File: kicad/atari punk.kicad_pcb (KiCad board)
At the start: 2 copper layers, 66 x 33 mm, 20 parts, among them J1 JACK_2P, J2 JACK_2P, J3 JACK_2P, P9v1 CONN_2, SW1 DUAL_SWITCH_INV, U1 LM555N, U2 LM555N

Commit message: Added missing tracks, made GND and Vin tracks 0.6mm.
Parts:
- moved R2 2.54 mm to (123.2, 101.6), turned to 270 degrees
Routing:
- net N-000001: track 6.66 -> 25.1 mm
- net GND: track 98.1 -> 108.6 mm
- net N-0000015: track 5.24 -> 7.40 mm
- net N-000004: track 10.4 -> 8.89 mm
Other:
- net class Vin added: clearance 0.254, trace_width 0.6, via_dia 0.889, via_drill 0.635
- net class gnd added: clearance 0.254, trace_width 0.6, via_dia 0.889, via_drill 0.635
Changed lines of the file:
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@@
   (general
     (links 32)
-    (no_connects 4)
-    (area 0 0 0 0)
+    (no_connects 0)
+    (area 113.674286 84.459334 181.20381 119.430001)
     (thickness 1.6)
     (drawings 6)
-    (tracks 50)
+    (tracks 55)
     (zones 0)
     (modules 20)
@@
       (outputformat 1)
       (mirror false)
-      (drillshape 1)
+      (drillshape 0)
       (scaleselection 1)
       (outputdirectory ""))
@@
     (add_net /OUTPUT_A)
     (add_net /OUTPUT_B)
-    (add_net /Vin)
-    (add_net GND)
     (add_net N-000001)
     (add_net N-0000012)
@@
     (add_net VCC)
   )
+  (net_class Vin ""
+    (clearance 0.254)
+    (trace_width 0.6)
+    (via_dia 0.889)
+    (via_drill 0.635)
+    (uvia_dia 0.508)
+    (uvia_drill 0.127)
+    (add_net /Vin)
+  )
+  (net_class gnd ""
+    (clearance 0.254)
+    (trace_width 0.6)
+    (via_dia 0.889)
+    (via_drill 0.635)
+    (uvia_dia 0.508)
+    (uvia_drill 0.127)
+    (add_net GND)
+  )
   (module R1 (layer F.Cu)
-    (at 123.19 99.06 90)
+    (at 123.19 101.6 270)
     (descr "Resistance verticale")
     (tags R)
     (autoplace_cost90 10)
     (autoplace_cost180 10)
-    (fp_text reference R2 (at -1.016 2.54 90) (layer F.SilkS)
+    (fp_text reference R2 (at -1.016 2.54 270) (layer F.SilkS)
       (effects (font (size 1.397 1.27) (thickness 0.2032)))
     )
-    (fp_text value 1k (at -1.143 2.54 90) (layer F.SilkS) hide
+    (fp_text value 1k (at -1.143 2.54 270) (layer F.SilkS) hide
       (effects (font (size 1.397 1.27) (thickness 0.2032)))
     )
     (fp_line (start -1.27 0) (end 1.27 0) (layer F.SilkS) (width 0.381))
     (fp_circle (center -1.27 0) (end -0.635 1.27) (layer F.SilkS) (width 0.381))
-    (pad 1 thru_hole circle (at -1.27 0 90) (size 1.397 1.397) (drill 0.8128)
+    (pad 1 thru_hole circle (at -1.27 0 270) (size 1.397 1.397) (drill 0.8128)
       (layers *.Cu *.Mask F.SilkS)
       (net 10 N-000002)
     )
-    (pad 2 thru_hole circle (at 1.27 0 90) (size 1.397 1.397) (drill 0.8128)
+    (pad 2 thru_hole circle (at 1.27 0 270) (size 1.397 1.397) (drill 0.8128)
       (layers *.Cu *.Mask F.SilkS)
       (net 5 N-000001)
@@
   (segment (start 138.43 100.33) (end 134.62 100.33) (width 0.254) (layer B.Cu) (net 1))
   (segment (start 157.48 101.6) (end 162.56 99.06) (width 0.254) (layer B.Cu) (net 2) (status 20))
-  (segment (start 168.91 90.17) (end 143.51 90.17) (width 0.254) (layer B.Cu) (net 3) (status 10))
-  (segment (start 162.56 114.3) (end 162.56 116.84) (width 0.254) (layer B.Cu) (net 4))
-  (segment (start 154.94 114.3) (end 154.94 116.84) (width 0.254) (layer B.Cu) (net 4))
-  (segment (start 163.83 116.84) (end 162.56 116.84) (width 0.254) (layer B.Cu) (net 4))
-  (segment (start 171.45 92.71) (end 171.45 109.22) (width 0.254) (layer B.Cu) (net 4))
-  (segment (start 171.45 109.22) (end 171.45 116.84) (width 0.254) (layer B.Cu) (net 4))
-  (segment (start 171.45 116.84) (end 163.83 116.84) (width 0.254) (layer B.Cu) (net 4))
-  (segment (start 162.56 116.84) (end 154.94 116.84) (width 0.254) (layer B.Cu) (net 4))
-  (segment (start 154.94 116.84) (end 134.62 116.84) (width 0.254) (layer B.Cu) (net 4))
-  (segment (start 134.62 116.84) (end 134.62 114.3) (width 0.254) (layer B.Cu) (net 4) (status 20))
-  (segment (start 171.45 92.71) (end 171.45 90.17) (width 0.254) (layer B.Cu) (net 4))
-  (segment (start 162.56 92.71) (end 171.45 92.71) (width 0.254) (layer B.Cu) (net 4))
-  (segment (start 162.56 114.3) (end 157.48 106.68) (width 0.254) (layer B.Cu) (net 4) (status 10))
+  (segment (start 143.51 90.17) (end 168.91 90.17) (width 0.6) (layer B.Cu) (net 3) (status C00000))
+  (segment (start 162.56 107.95) (end 158.75 107.95) (width 0.6) (layer B.Cu) (net 4) (status 400000))
+  (segment (start 158.75 107.95) (end 157.48 106.68) (width 0.6) (layer B.Cu) (net 4) (status 800000))
+  (segment (start 154.94 114.3) (end 154.94 116.84) (width 0.6) (layer B.Cu) (net 4) (status 400000))
+  (segment (start 162.56 116.84) (end 162.56 114.3) (width 0.6) (layer B.Cu) (net 4) (status 800000))
+  (segment (start 134.62 114.3) (end 134.62 105.41) (width 0.6) (layer B.Cu) (net 4) (status C00000))
+  (segment (start 171.45 90.17) (end 171.45 116.84) (width 0.6) (layer B.Cu) (net 4) (status 400000))
+  (segment (start 134.62 116.84) (end 134.62 114.3) (width 0.6) (layer B.Cu) (net 4) (status 800000))
+  (segment (start 171.45 116.84) (end 162.56 116.84) (width 0.6) (layer B.Cu) (net 4))
+  (segment (start 162.56 116.84) (end 154.94 116.84) (width 0.6) (layer B.Cu) (net 4))
+  (segment (start 154.94 116.84) (end 134.62 116.84) (width 0.6) (layer B.Cu) (net 4))
+  (segment (start 171.45 90.17) (end 171.45 92.71) (width 0.6) (layer B.Cu) (net 4) (status 400000))
+  (segment (start 171.45 92.71) (end 162.56 92.71) (width 0.6) (layer B.Cu) (net 4) (status 800000))
+  (segment (start 162.56 114.3) (end 162.56 111.76) (width 0.6) (layer B.Cu) (net 4) (status 400000))
+  (segment (start 162.56 111.76) (end 157.48 106.68) (width 0.6) (layer B.Cu) (net 4) (status 800000))
+  (segment (start 158.75 107.95) (end 157.48 106.68) (width 0.254) (layer B.Cu) (net 4))
   (segment (start 134.62 114.3) (end 134.62 114.3) (width 0.254) (layer B.Cu) (net 4) (status 30))
-  (segment (start 134.62 105.41) (end 134.62 114.3) (width 0.254) (layer B.Cu) (net 4) (status 20))
-  (segment (start 123.19 97.79) (end 123.19 96.52) (width 0.254) (layer B.Cu) (net 5))
+  (segment (start 127 102.87) (end 130.81 99.06) (width 0.254) (layer B.Cu) (net 5))
+  (segment (start 130.81 96.52) (end 127 92.71) (width 0.254) (layer B.Cu) (net 5))
+  (segment (start 130.81 99.06) (end 130.81 96.52) (width 0.254) (layer B.Cu) (net 5))
   (segment (start 123.19 96.52) (end 127 92.71) (width 0.254) (layer B.Cu) (net 5))
+  (segment (start 123.19 102.87) (end 123.19 96.52) (width 0.254) (layer B.Cu) (net 5) (status 10))
   (segment (start 143.51 104.14) (end 149.86 104.14) (width 0.254) (layer B.Cu) (net 6))
   (segment (start 143.51 109.22) (end 143.51 104.14) (width 0.254) (layer B.Cu) (net 6) (status 10))
@@
   (segment (start 143.51 114.3) (end 149.86 114.3) (width 0.254) (layer B.Cu) (net 7) (status 20))
   (segment (start 123.19 113.03) (end 129.54 114.3) (width 0.254) (layer B.Cu) (net 8) (status 20))
+  (segment (start 167.64 114.3) (end 167.64 110.49) (width 0.254) (layer B.Cu) (net 9))
+  (segment (start 167.64 110.49) (end 165.1 107.95) (width 0.254) (layer B.Cu) (net 9))
   (segment (start 167.64 114.3) (end 167.64 114.3) (width 0.254) (layer B.Cu) (net 9) (status 30))
-  (segment (start 165.1 107.95) (end 166.37 102.87) (width 0.254) (layer B.Cu) (net 9) (status 10))
-  (segment (start 127 100.33) (end 123.19 100.33) (width 0.254) (layer B.Cu) (net 10))
+  (segment (start 127 100.33) (end 123.19 100.33) (width 0.254) (layer B.Cu) (net 10) (status 20))
+  (segment (start 123.19 100.33) (end 123.19 110.49) (width 0.254) (layer B.Cu) (net 10) (status 10))
   (segment (start 134.62 102.87) (end 133.35 102.87) (width 0.254) (layer B.Cu) (net 10))
   (segment (start 123.19 110.49) (end 123.19 110.49) (width 0.254) (layer B.Cu) (net 10) (status 30))
@@
   (segment (start 130.81 105.41) (end 130.81 110.49) (width 0.254) (layer B.Cu) (net 10))
   (segment (start 133.35 102.87) (end 130.81 105.41) (width 0.254) (layer B.Cu) (net 10))
-  (segment (start 123.19 100.33) (end 123.19 110.49) (width 0.254) (layer B.Cu) (net 10) (status 20))
-  (segment (start 167.64 114.3) (end 167.64 107.95) (width 0.254) (layer B.Cu) (net 11) (status 10))
-  (segment (start 166.37 102.87) (end 167.64 99.06) (width 0.254) (layer B.Cu) (net 11) (status 20))
+  (segment (start 167.64 99.06) (end 167.64 107.95) (width 0.254) (layer B.Cu) (net 11))
   (segment (start 153.67 92.71) (end 160.02 92.71) (width 0.254) (layer B.Cu) (net 12))
   (segment (start 129.54 92.71) (end 132.08 92.71) (width 0.254) (layer B.Cu) (net 13))

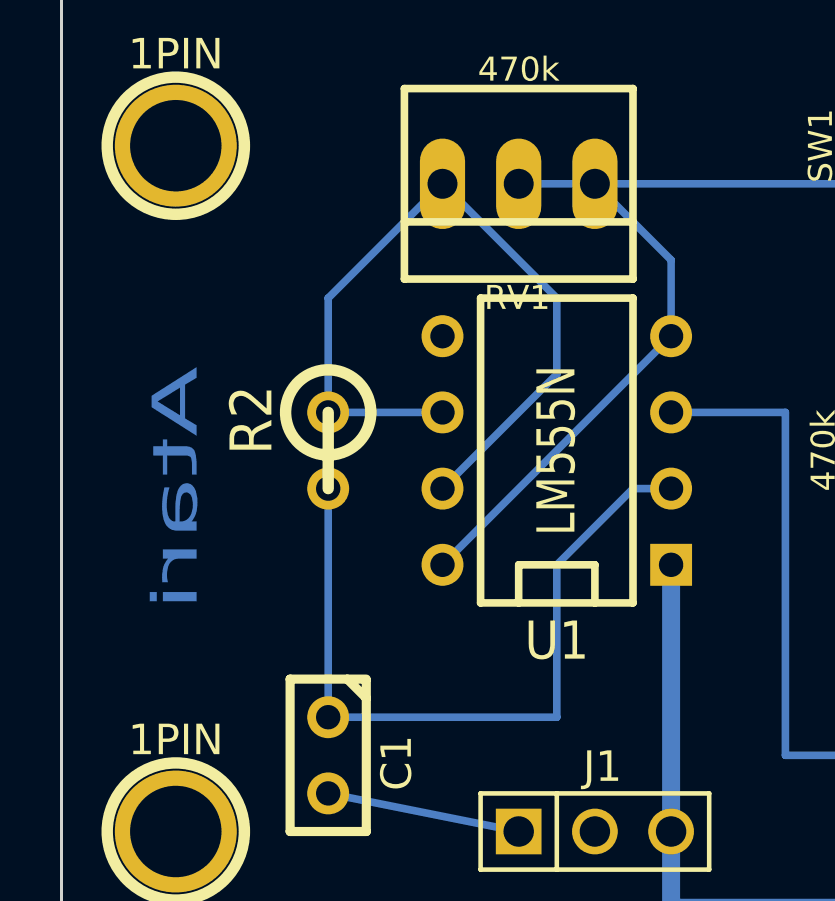
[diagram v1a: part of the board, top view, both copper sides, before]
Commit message: Fixed a bad track at R2.
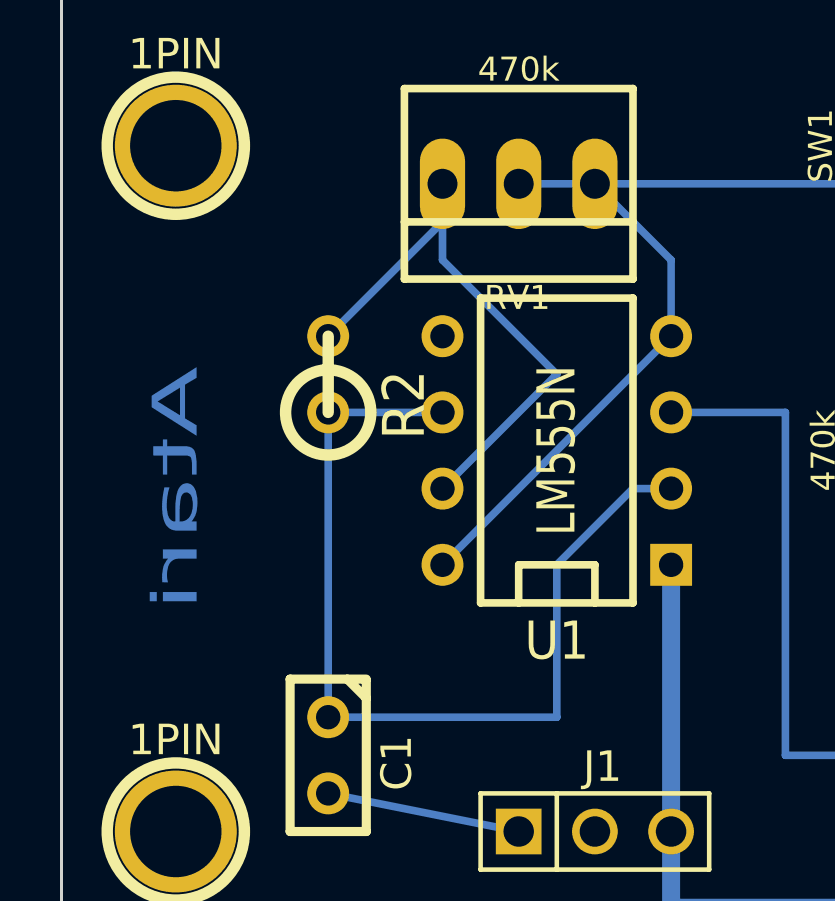
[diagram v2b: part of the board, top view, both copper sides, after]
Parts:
- moved R2 2.54 mm to (123.2, 99.1), turned to 90 degrees
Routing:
- net N-000001: track 25.1 -> 20.0 mm
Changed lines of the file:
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@@
   )
   (module R1 (layer F.Cu)
-    (at 123.19 101.6 270)
+    (at 123.19 99.06 90)
     (descr "Resistance verticale")
     (tags R)
     (autoplace_cost90 10)
     (autoplace_cost180 10)
-    (fp_text reference R2 (at -1.016 2.54 270) (layer F.SilkS)
+    (fp_text reference R2 (at -1.016 2.54 90) (layer F.SilkS)
       (effects (font (size 1.397 1.27) (thickness 0.2032)))
     )
-    (fp_text value 1k (at -1.143 2.54 270) (layer F.SilkS) hide
+    (fp_text value 1k (at -1.143 2.54 90) (layer F.SilkS) hide
       (effects (font (size 1.397 1.27) (thickness 0.2032)))
     )
     (fp_line (start -1.27 0) (end 1.27 0) (layer F.SilkS) (width 0.381))
     (fp_circle (center -1.27 0) (end -0.635 1.27) (layer F.SilkS) (width 0.381))
-    (pad 1 thru_hole circle (at -1.27 0 270) (size 1.397 1.397) (drill 0.8128)
+    (pad 1 thru_hole circle (at -1.27 0 90) (size 1.397 1.397) (drill 0.8128)
       (layers *.Cu *.Mask F.SilkS)
       (net 10 N-000002)
     )
-    (pad 2 thru_hole circle (at 1.27 0 270) (size 1.397 1.397) (drill 0.8128)
+    (pad 2 thru_hole circle (at 1.27 0 90) (size 1.397 1.397) (drill 0.8128)
       (layers *.Cu *.Mask F.SilkS)
       (net 5 N-000001)
@@
   (segment (start 138.43 100.33) (end 134.62 100.33) (width 0.254) (layer B.Cu) (net 1))
   (segment (start 157.48 101.6) (end 162.56 99.06) (width 0.254) (layer B.Cu) (net 2) (status 20))
-  (segment (start 143.51 90.17) (end 168.91 90.17) (width 0.6) (layer B.Cu) (net 3) (status C00000))
-  (segment (start 162.56 107.95) (end 158.75 107.95) (width 0.6) (layer B.Cu) (net 4) (status 400000))
-  (segment (start 158.75 107.95) (end 157.48 106.68) (width 0.6) (layer B.Cu) (net 4) (status 800000))
-  (segment (start 154.94 114.3) (end 154.94 116.84) (width 0.6) (layer B.Cu) (net 4) (status 400000))
-  (segment (start 162.56 116.84) (end 162.56 114.3) (width 0.6) (layer B.Cu) (net 4) (status 800000))
-  (segment (start 134.62 114.3) (end 134.62 105.41) (width 0.6) (layer B.Cu) (net 4) (status C00000))
-  (segment (start 171.45 90.17) (end 171.45 116.84) (width 0.6) (layer B.Cu) (net 4) (status 400000))
-  (segment (start 134.62 116.84) (end 134.62 114.3) (width 0.6) (layer B.Cu) (net 4) (status 800000))
+  (segment (start 143.51 90.17) (end 168.91 90.17) (width 0.6) (layer B.Cu) (net 3))
+  (segment (start 162.56 107.95) (end 158.75 107.95) (width 0.6) (layer B.Cu) (net 4))
+  (segment (start 158.75 107.95) (end 157.48 106.68) (width 0.6) (layer B.Cu) (net 4))
+  (segment (start 154.94 114.3) (end 154.94 116.84) (width 0.6) (layer B.Cu) (net 4))
+  (segment (start 162.56 116.84) (end 162.56 114.3) (width 0.6) (layer B.Cu) (net 4))
+  (segment (start 134.62 114.3) (end 134.62 105.41) (width 0.6) (layer B.Cu) (net 4))
+  (segment (start 171.45 90.17) (end 171.45 116.84) (width 0.6) (layer B.Cu) (net 4))
+  (segment (start 134.62 116.84) (end 134.62 114.3) (width 0.6) (layer B.Cu) (net 4))
   (segment (start 171.45 116.84) (end 162.56 116.84) (width 0.6) (layer B.Cu) (net 4))
   (segment (start 162.56 116.84) (end 154.94 116.84) (width 0.6) (layer B.Cu) (net 4))
   (segment (start 154.94 116.84) (end 134.62 116.84) (width 0.6) (layer B.Cu) (net 4))
-  (segment (start 171.45 90.17) (end 171.45 92.71) (width 0.6) (layer B.Cu) (net 4) (status 400000))
-  (segment (start 171.45 92.71) (end 162.56 92.71) (width 0.6) (layer B.Cu) (net 4) (status 800000))
-  (segment (start 162.56 114.3) (end 162.56 111.76) (width 0.6) (layer B.Cu) (net 4) (status 400000))
-  (segment (start 162.56 111.76) (end 157.48 106.68) (width 0.6) (layer B.Cu) (net 4) (status 800000))
+  (segment (start 171.45 90.17) (end 171.45 92.71) (width 0.6) (layer B.Cu) (net 4))
+  (segment (start 171.45 92.71) (end 162.56 92.71) (width 0.6) (layer B.Cu) (net 4))
+  (segment (start 162.56 114.3) (end 162.56 111.76) (width 0.6) (layer B.Cu) (net 4))
+  (segment (start 162.56 111.76) (end 157.48 106.68) (width 0.6) (layer B.Cu) (net 4))
   (segment (start 158.75 107.95) (end 157.48 106.68) (width 0.254) (layer B.Cu) (net 4))
   (segment (start 134.62 114.3) (end 134.62 114.3) (width 0.254) (layer B.Cu) (net 4) (status 30))
-  (segment (start 127 102.87) (end 130.81 99.06) (width 0.254) (layer B.Cu) (net 5))
-  (segment (start 130.81 96.52) (end 127 92.71) (width 0.254) (layer B.Cu) (net 5))
-  (segment (start 130.81 99.06) (end 130.81 96.52) (width 0.254) (layer B.Cu) (net 5))
-  (segment (start 123.19 96.52) (end 127 92.71) (width 0.254) (layer B.Cu) (net 5))
-  (segment (start 123.19 102.87) (end 123.19 96.52) (width 0.254) (layer B.Cu) (net 5) (status 10))
+  (segment (start 127 92.71) (end 127 95.25) (width 0.254) (layer B.Cu) (net 5))
+  (segment (start 130.81 99.06) (end 127 102.87) (width 0.254) (layer B.Cu) (net 5))
+  (segment (start 127 95.25) (end 130.81 99.06) (width 0.254) (layer B.Cu) (net 5))
+  (segment (start 127 92.71) (end 127 93.98) (width 0.254) (layer B.Cu) (net 5))
+  (segment (start 127 93.98) (end 123.19 97.79) (width 0.254) (layer B.Cu) (net 5))
   (segment (start 143.51 104.14) (end 149.86 104.14) (width 0.254) (layer B.Cu) (net 6))
   (segment (start 143.51 109.22) (end 143.51 104.14) (width 0.254) (layer B.Cu) (net 6) (status 10))
@@
   (segment (start 167.64 110.49) (end 165.1 107.95) (width 0.254) (layer B.Cu) (net 9))
   (segment (start 167.64 114.3) (end 167.64 114.3) (width 0.254) (layer B.Cu) (net 9) (status 30))
-  (segment (start 127 100.33) (end 123.19 100.33) (width 0.254) (layer B.Cu) (net 10) (status 20))
-  (segment (start 123.19 100.33) (end 123.19 110.49) (width 0.254) (layer B.Cu) (net 10) (status 10))
+  (segment (start 127 100.33) (end 123.19 100.33) (width 0.254) (layer B.Cu) (net 10))
+  (segment (start 123.19 110.49) (end 123.19 100.33) (width 0.254) (layer B.Cu) (net 10))
   (segment (start 134.62 102.87) (end 133.35 102.87) (width 0.254) (layer B.Cu) (net 10))
   (segment (start 123.19 110.49) (end 123.19 110.49) (width 0.254) (layer B.Cu) (net 10) (status 30))
